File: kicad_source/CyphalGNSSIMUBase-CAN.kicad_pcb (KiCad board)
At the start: 2 copper layers, 52 x 36 mm, 73 parts, among them CN1 SM04B-SRSS-TB, CN2 Conn_01x03, CN3 RASPBERRYPI_PICO, CN4 SM04B-GHS-TB, CN5 SM04B-GHS-TB, SW1 PTS636 SM43 SMTR LFS, U1 M24C64-RMN6TP, U2 MCP2515T-I/SO, U3 SN65HVD230, U4 BNO085, U5 MAX3232, U6 MAX-M10S, Y1 X322516MLB4SI, Y2 DNI

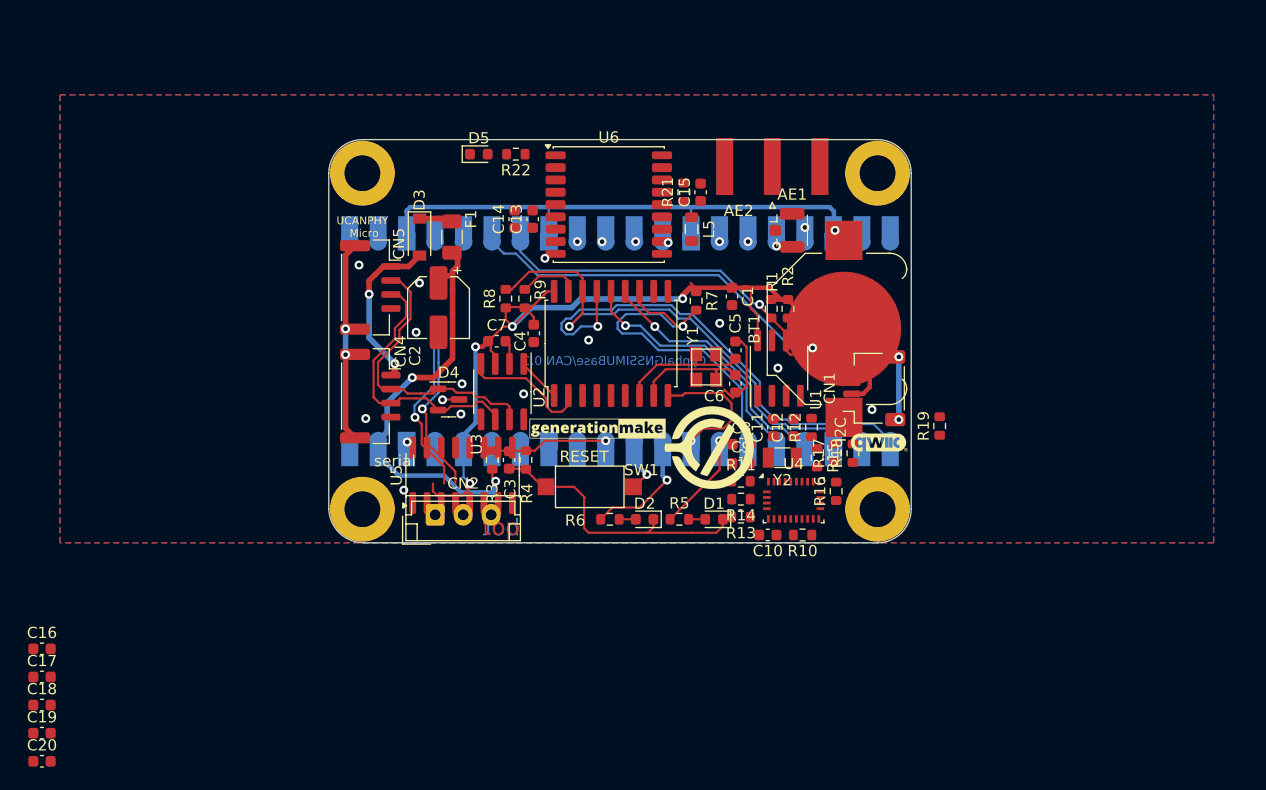
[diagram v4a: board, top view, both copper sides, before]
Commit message: connected reset of BNO055 and GNSS module, updated layout
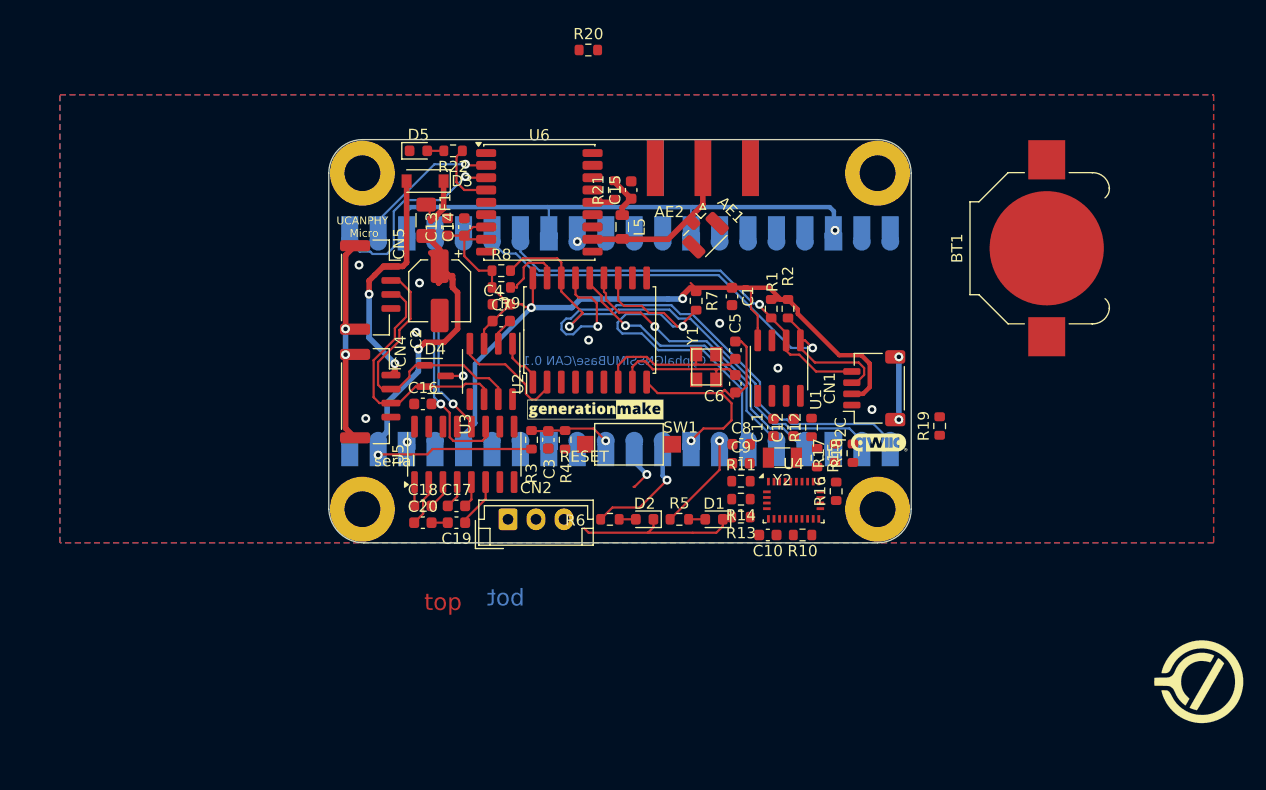
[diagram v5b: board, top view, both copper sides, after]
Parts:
- added R20: 10k, Resistor_SMD:R_0603_1608Metric, F.Cu at (87.2, 66.0)
- moved L3 48.4 mm to (141.7, 122.4)
- moved C19 41.5 mm to (75.4, 108.2), turned to 180 degrees
- moved C16 40.4 mm to (72.4, 97.6)
- moved C20 40.1 mm to (72.4, 108.2)
- moved C17 40.0 mm to (75.4, 106.7)
- moved C18 38.4 mm to (72.4, 106.7)
- moved BT1 19.5 mm to (128.1, 83.7)
- moved C13 7.63 mm to (74.6, 81.8)
- moved AE1 7.60 mm to (97.3, 82.2), turned to -45 degrees
- moved CN2 6.51 mm to (80.0, 107.9)
- moved C15 6.20 mm to (91.0, 78.5)
- moved L5 6.20 mm to (90.2, 81.8)
- moved R21 6.20 mm to (89.5, 78.5)
- moved U6 6.20 mm to (82.8, 79.6)
- moved AE2 6.20 mm to (97.4, 76.5)
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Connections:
- net /GNSS/D2_R renamed /GNSS/D5_R
- net Net-(C15-Pad1) renamed /GNSS/VCC_RF_R
- net Net-(U5-C1+) renamed /RS232_C1+
- net Net-(U5-C1-) renamed /RS232_C1-
- net Net-(U5-C2+) renamed /RS232_C2+
- net Net-(U5-C2-) renamed /RS232_C2-
- CN3 pad 10: /INPUT1 -> GNSS_RESET
- CN3 pad 14: /OUTPUT0 -> unconnected-(CN3-GP10/SPI1_SCK/I2C1_SDA-Pad14)
- CN3 pad 15: /OUTPUT1 -> unconnected-(CN3-GP11/SPI1_TX/I2C1_SCL-Pad15)_1
- CN3 pad 16: /RESERVED0 -> unconnected-(CN3-GP12/SPI1_RX/I2C0_SDA/UART0_TX-Pad16)
- CN3 pad 17: /NEOPIXEL -> unconnected-(CN3-GP13/SPI1_CS/I2C0_SCL/UART0_RX-Pad17)
- CN3 pad 19: /SERVO0 -> unconnected-(CN3-GP14/SPI1_SCK/I2C1_SDA-Pad19)
- CN3 pad 20: /SERVO1 -> unconnected-(CN3-GP15/SPI1_TX/I2C1_SCL-Pad20)
- CN3 pad 32: /ANALOG_INPUT0 -> unconnected-(CN3-GP27/ADC1/I2C1_SCL-Pad32)_1
- CN3 pad 34: /ANALOG_INPUT1 -> unconnected-(CN3-GP28/ADC2-Pad34)_1
- CN3 pad 9: /INPUT0 -> BNO_RESET
- U4 pad 11: /BNO085/RESET -> BNO_RESET
- U6 pad 9: /GNSS/NEO_RESET -> GNSS_RESET
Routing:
- net SERIAL1_TX: track 1.27 -> 18.7 mm, vias 0 -> 1
- net /GNSS/NEO_ANTENNA: track 1.27 -> 14.4 mm, vias 1 -> 0
- net SERIAL1_RX: track 1.27 -> 13.6 mm, vias 0 -> 1
- net (no net): track 6.35 -> 15.2 mm
- net +BATT: track 37.9 -> 44.1 mm
- net GND: track 94.6 -> 88.3 mm, vias 17 -> 12
- net /GNSS/TIMEPULSE: track 0.00 -> 5.96 mm
- net /MCP2515/CANVCC: track 15.0 -> 20.8 mm
- net Net-(U5-VS-): track 0.00 -> 4.38 mm
- net /SERIAL2_RX: track 16.0 -> 11.7 mm
- net Net-(U5-VS+): track 0.00 -> 4.16 mm
- net /GNSS/VCC_RF_R: track 0.00 -> 4.02 mm
- net SCK: track 24.3 -> 27.5 mm
- net /+BATT_MEAS: track 11.8 -> 8.78 mm
- net MCP2515_INT: track 34.4 -> 37.3 mm
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
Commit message: updated layout
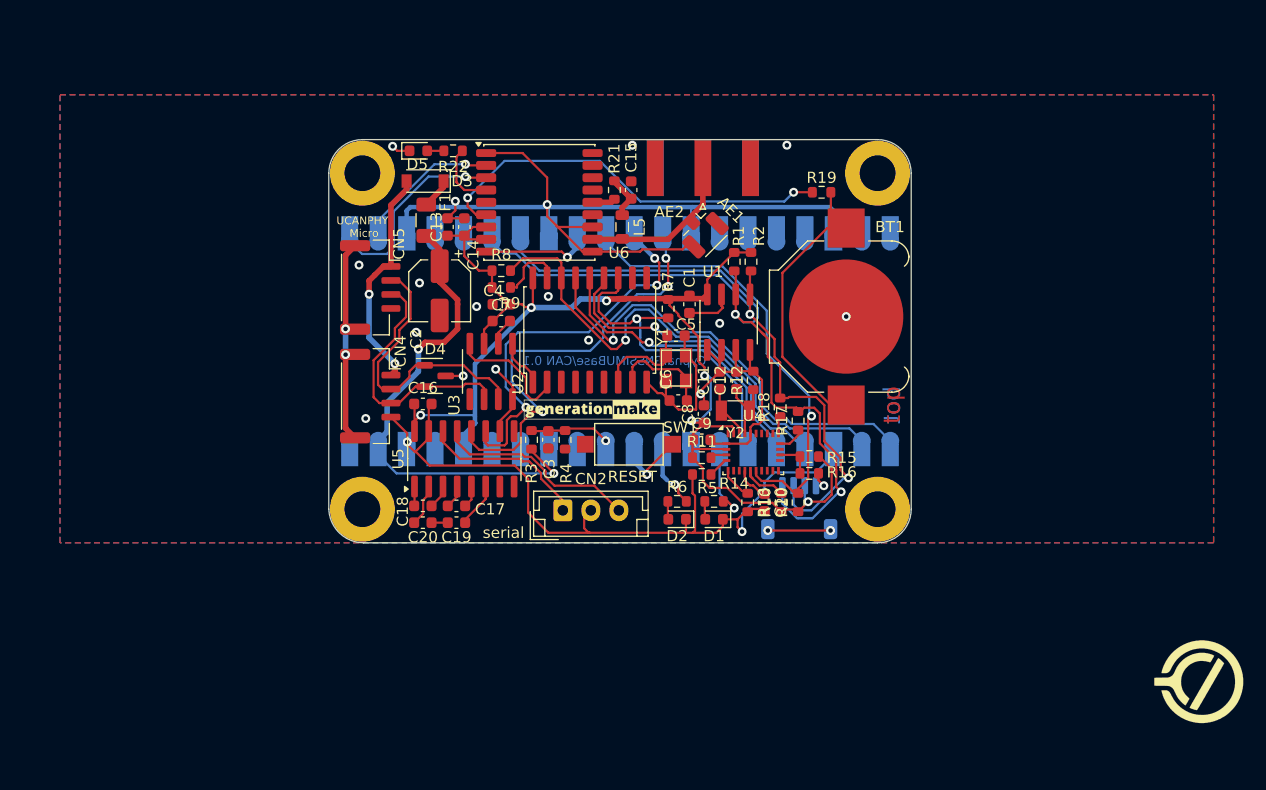
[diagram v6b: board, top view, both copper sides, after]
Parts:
- CN1, L4: moved to B.Cu
- moved R20 44.5 mm to (105.9, 106.4), turned to 90 degrees
- moved R19 23.4 mm to (108.0, 78.7), turned to 180 degrees
- moved BT1 18.9 mm to (110.2, 89.8)
- moved L4 17.1 mm to (97.8, 108.7), turned to 180 degrees
- moved CN1 12.6 mm to (106.0, 106.9), turned to 180 degrees
- moved L2 12.5 mm to (77.1, 110.7)
- moved R18 7.69 mm to (104.3, 97.9)
- moved R12 6.68 mm to (101.9, 95.5)
- moved C12 6.61 mm to (100.4, 95.5)
- moved C11 6.38 mm to (98.9, 95.5)
- moved R6 6.21 mm to (95.1, 106.3), turned to 180 degrees
- moved U1 6.09 mm to (99.7, 90.3)
- moved Y2 5.94 mm to (100.3, 98.2)
- moved U4 5.61 mm to (101.9, 101.9)
- moved C5 5.46 mm to (95.0, 91.5), turned to 0 degrees
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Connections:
- CN2 pad 3: /RS232_TX -> /RS232_RX
- CN3 pad 10: GNSS_RESET -> BNO_RESET
- CN3 pad 9: BNO_RESET -> GNSS_RESET
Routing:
- net GND: track 88.3 -> 208.4 mm, vias 12 -> 20
- net BNO_RESET: track 1.29 -> 41.6 mm
- net /GNSS/V_BCKP: track 0.00 -> 36.7 mm, vias 0 -> 2
- net +3V3: track 84.8 -> 118.4 mm, vias 2 -> 6
- net I2C_SCL: track 37.2 -> 65.7 mm, vias 1 -> 2
- net /SERIAL2_RX: track 11.7 -> 40.1 mm, vias 1 -> 3
- net /GNSS/V_BCKP_R: track 0.00 -> 26.1 mm
- net /SERIAL2_TX: track 16.2 -> 36.7 mm, vias 1 -> 3
- net /RS232_RX: track 0.00 -> 18.2 mm
- net /RS232_TX: track 0.00 -> 15.0 mm
- net I2C_SDA: track 46.8 -> 59.6 mm, vias 1 -> 2
- net GNSS_RESET: track 1.27 -> 10.5 mm, vias 0 -> 1
- net /BNO085/CLKSEL1: track 0.00 -> 6.62 mm
- net MCP2515_INT: track 37.3 -> 31.2 mm
- net MISO: track 47.6 -> 41.5 mm
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
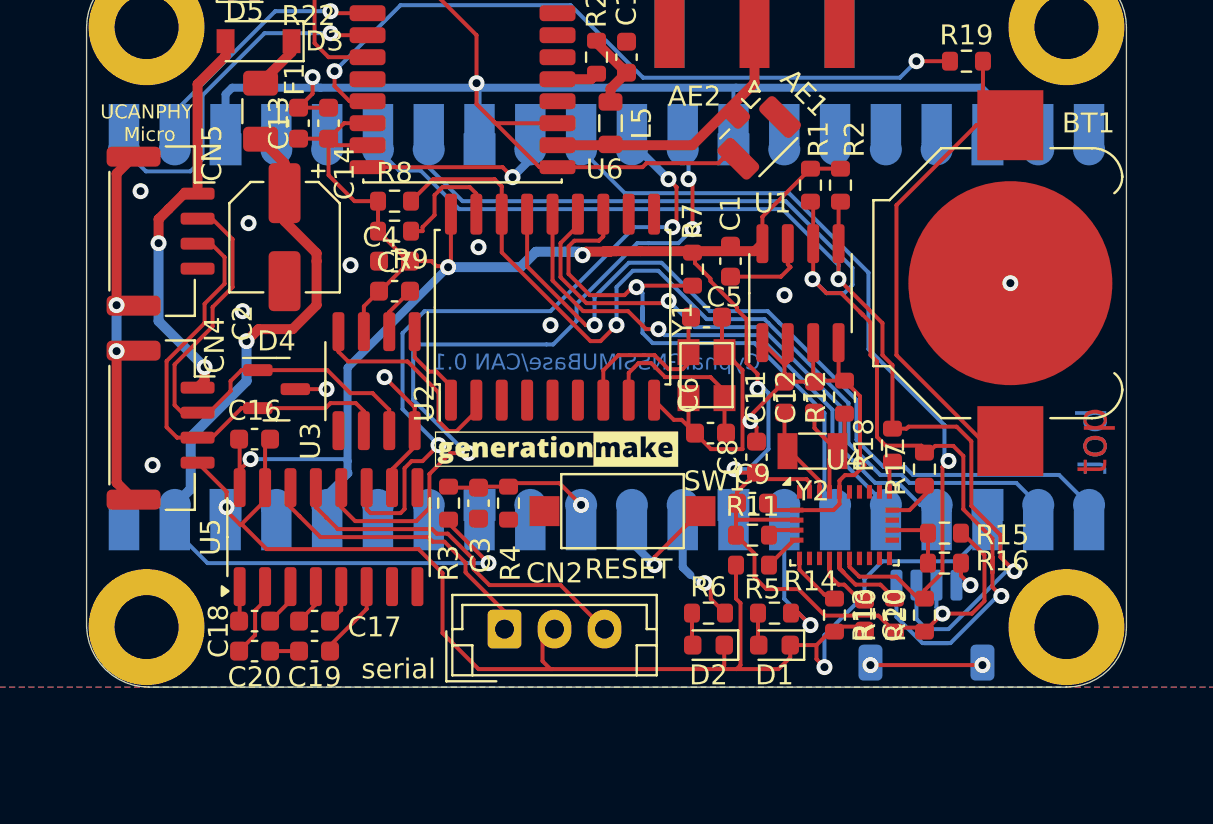
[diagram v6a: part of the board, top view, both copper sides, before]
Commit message: fixed some drc errors
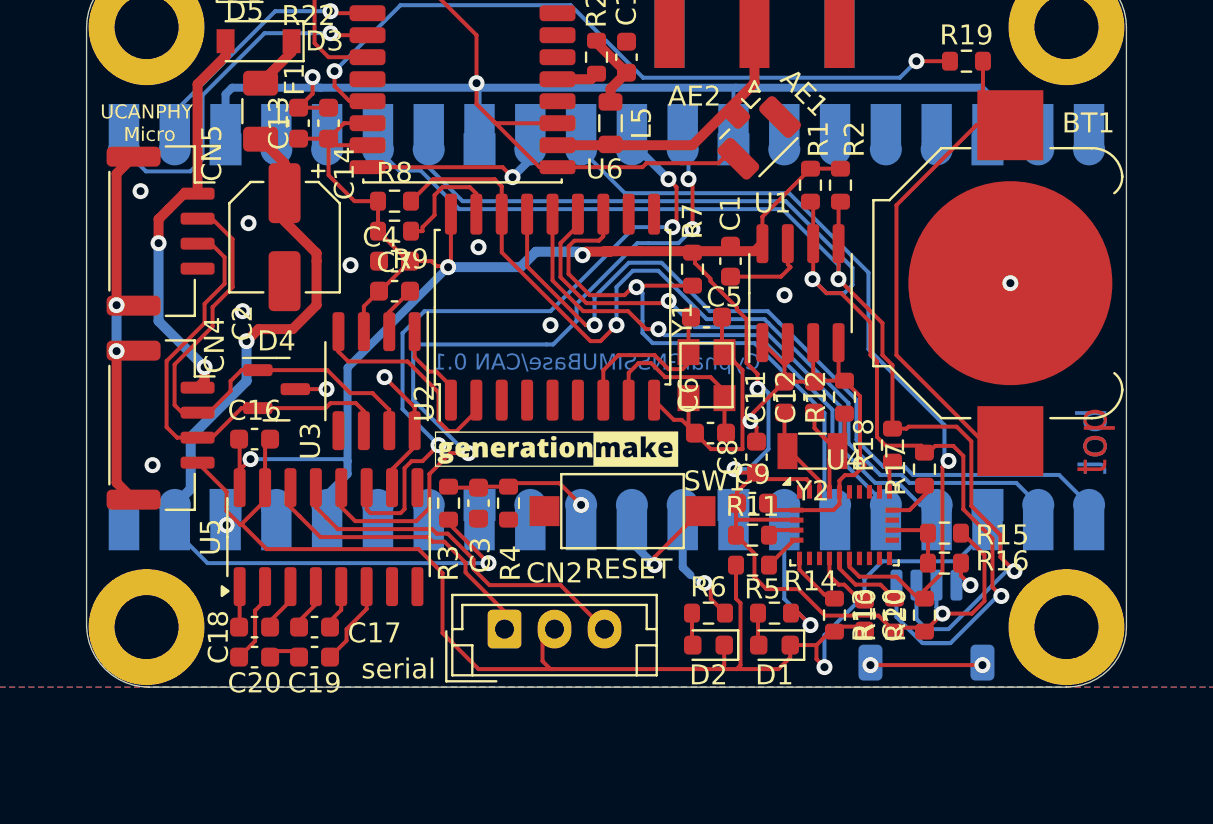
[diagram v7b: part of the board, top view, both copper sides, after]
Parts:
- moved C17 0.30 mm to (75.4, 107.0)
- moved C18 0.30 mm to (72.4, 107.0)
- moved C19 0.30 mm to (75.4, 108.5)
- moved C20 0.30 mm to (72.4, 108.5)
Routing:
- net (no net): track 15.2 -> 1.27 mm
- net I2C_SCL: track 65.7 -> 64.7 mm
- net MCP2515_INT: track 31.2 -> 30.5 mm
- net /BNO085/CAP: track 3.94 -> 3.37 mm
- net Net-(U5-VS+): track 4.16 -> 4.66 mm

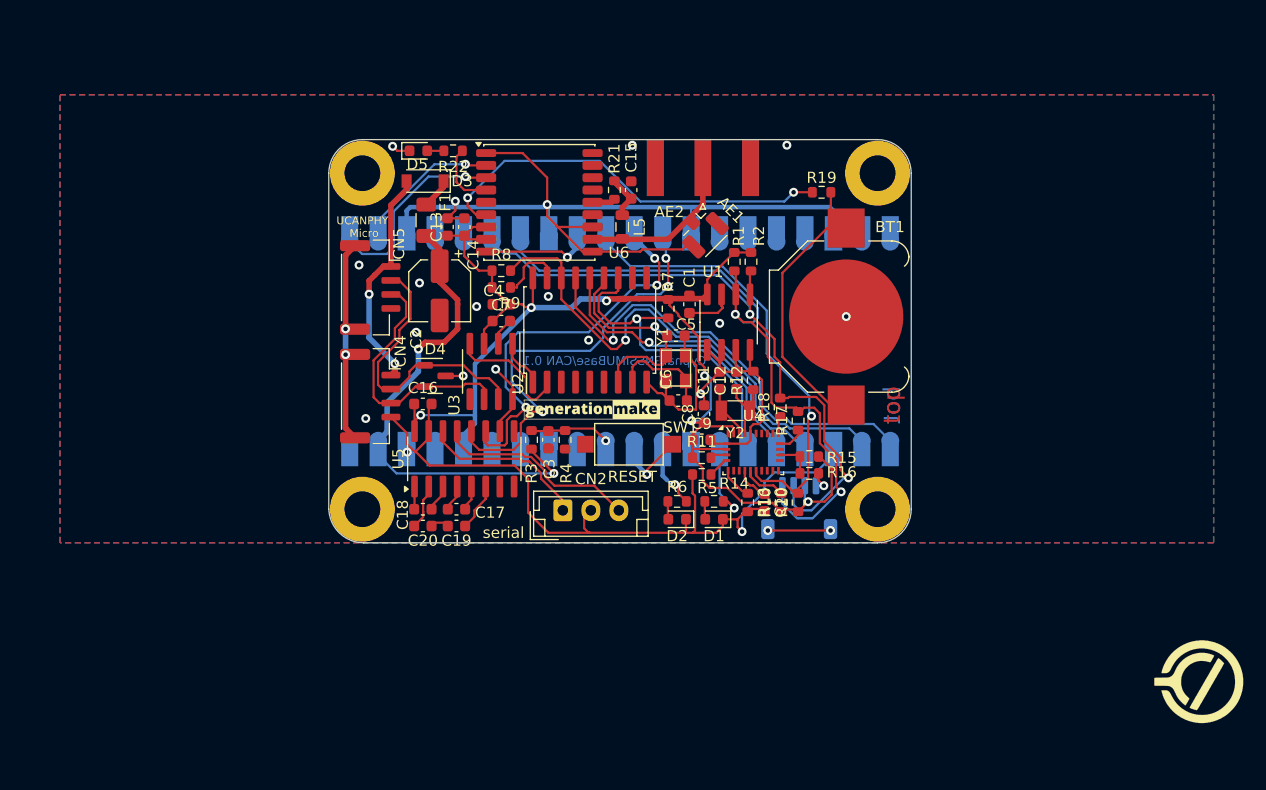
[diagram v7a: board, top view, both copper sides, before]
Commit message: fixed drc errors
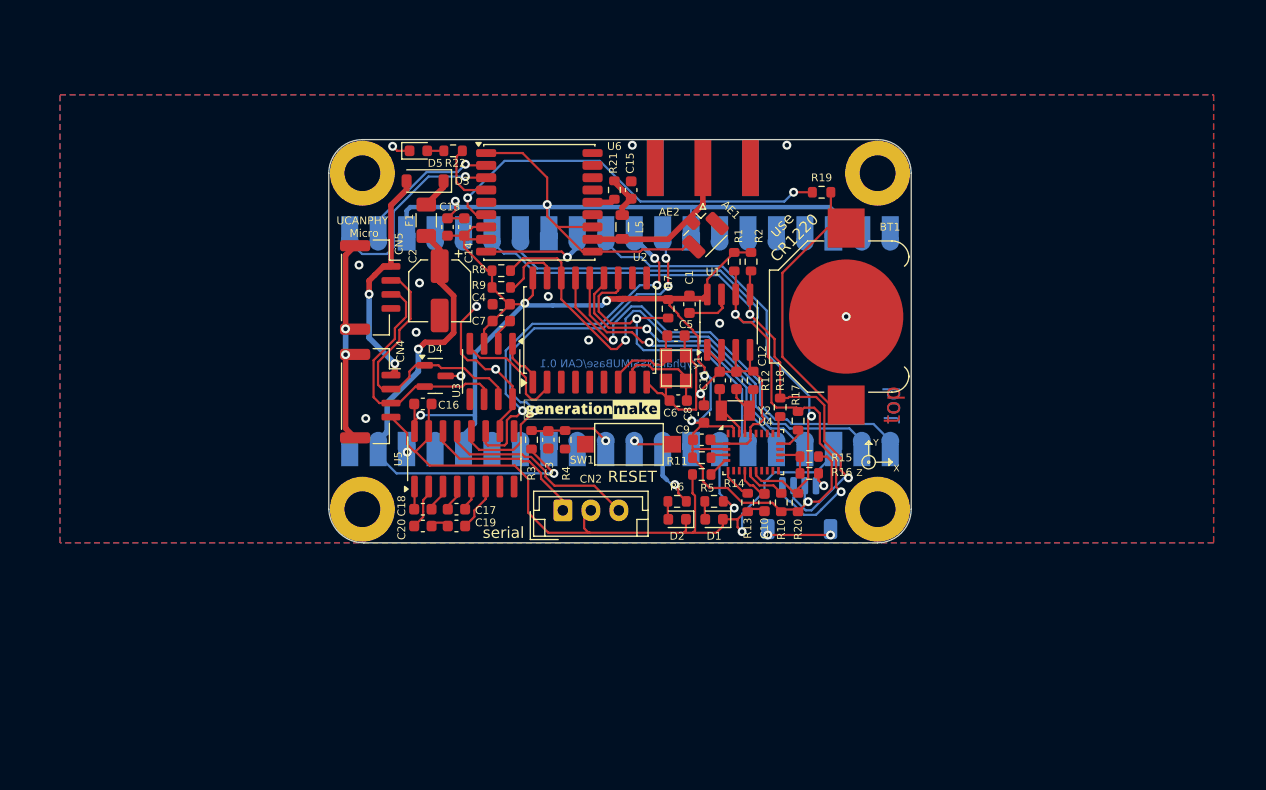
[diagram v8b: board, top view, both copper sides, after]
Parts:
- CN3: footprint generationmake:RASPI_PICO_SOLDER_Kopie -> generationmake:RASPI_PICO_SOLDER_ONLY
- L3: moved to B.Cu
- moved L3 45.3 mm to (110.2, 89.8), turned to 180 degrees
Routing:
- net GND: track 208.4 -> 216.8 mm
- net /RESET: track 7.13 -> 3.52 mm
- net I2C_SCL: track 64.7 -> 62.8 mm
- net +3V3: track 118.3 -> 116.8 mm
- net (no net): track 1.27 -> 0.00 mm
- net /SERIAL2_RX: track 40.1 -> 38.9 mm
- net /MCP2515/MCP2515_OSC2: track 8.83 -> 8.07 mm
- net /SERIAL2_TX: track 36.7 -> 36.2 mm
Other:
- board text added: "RX - GND - TX"
- board text added: "X"
- board text added: "Y"
- board text added: "Z"
- board text added: "use CR1220"
